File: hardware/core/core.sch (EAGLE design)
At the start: 520 parts, among them IC1 MAX481CSA, IC10 MAX481CSA, IC11 MAX481CSA, IC12 MAX481CSA, IC13 MAX481CSA, IC14 MAX481CSA, IC15 MAX481CSA, IC16 MAX481CSA, IC17 MAX481CSA, IC18 MAX481CSA, IC19 MAX481CSA, IC2 LD117AS12TR, IC20 MAX481CSA, IC21 MAX481CSA, IC22 LD117AS12TR, IC23 LD117AS12TR, IC3 MAX481CSA, IC4 MAX481CSA, IC5 MAX481CSA, IC6 MAX481CSA, IC7 MAX481CSA, IC8 MAX481CSA, IC9 MAX481CSA

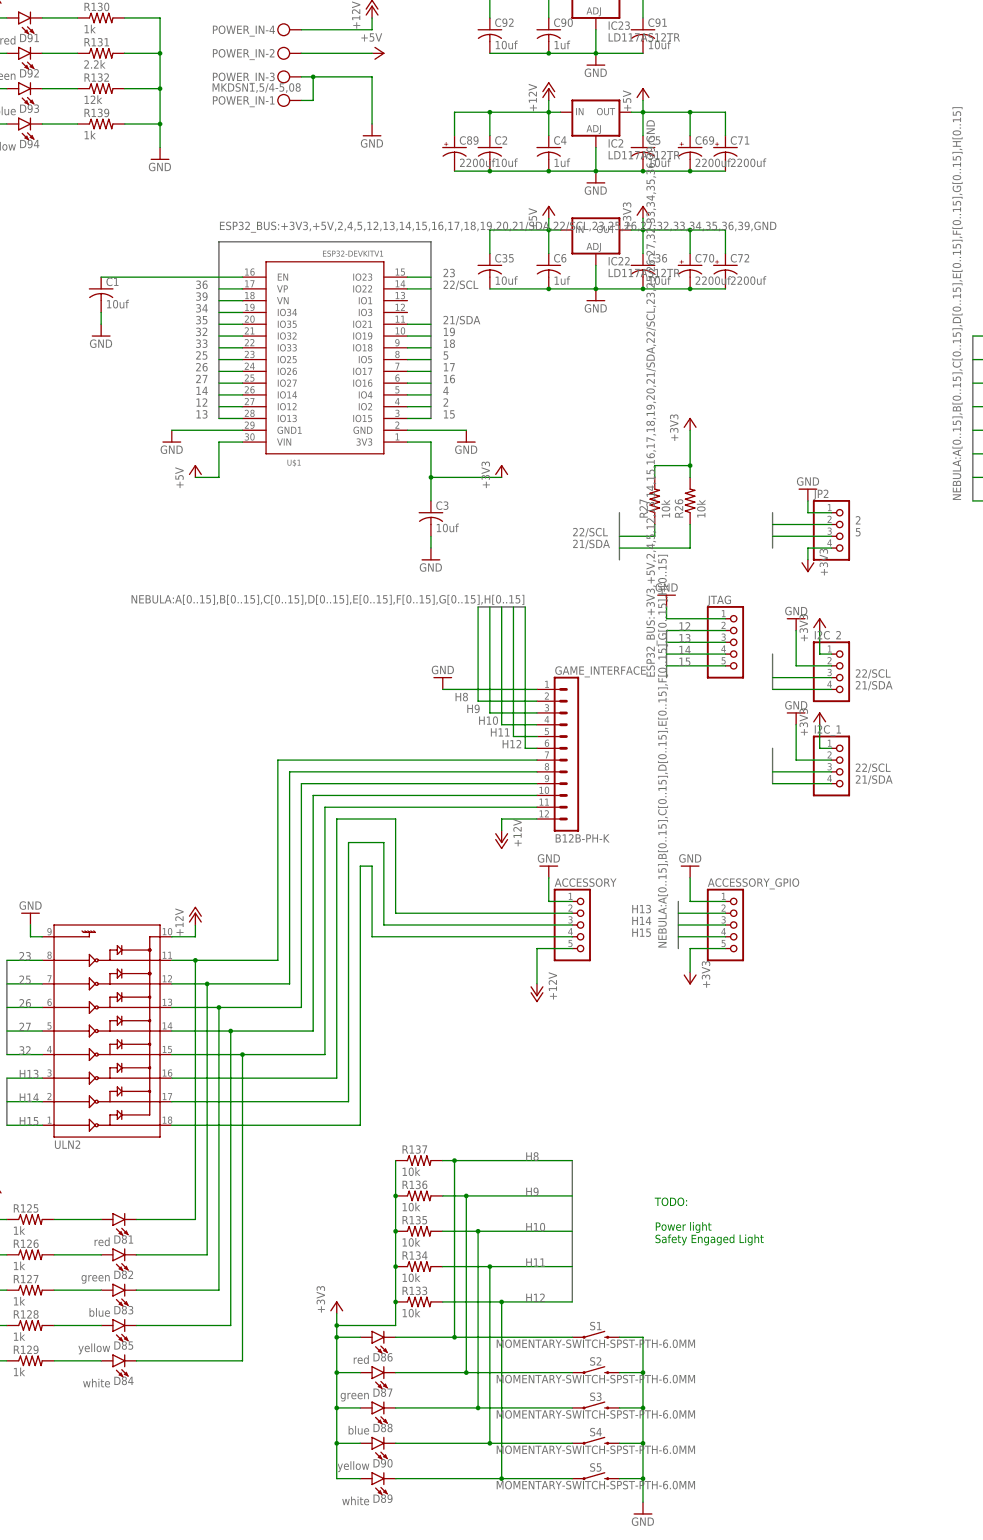
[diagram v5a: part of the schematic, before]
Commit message: Fix for button status resistors & 12v status dim
Fix for button status resistors & 12v status dim
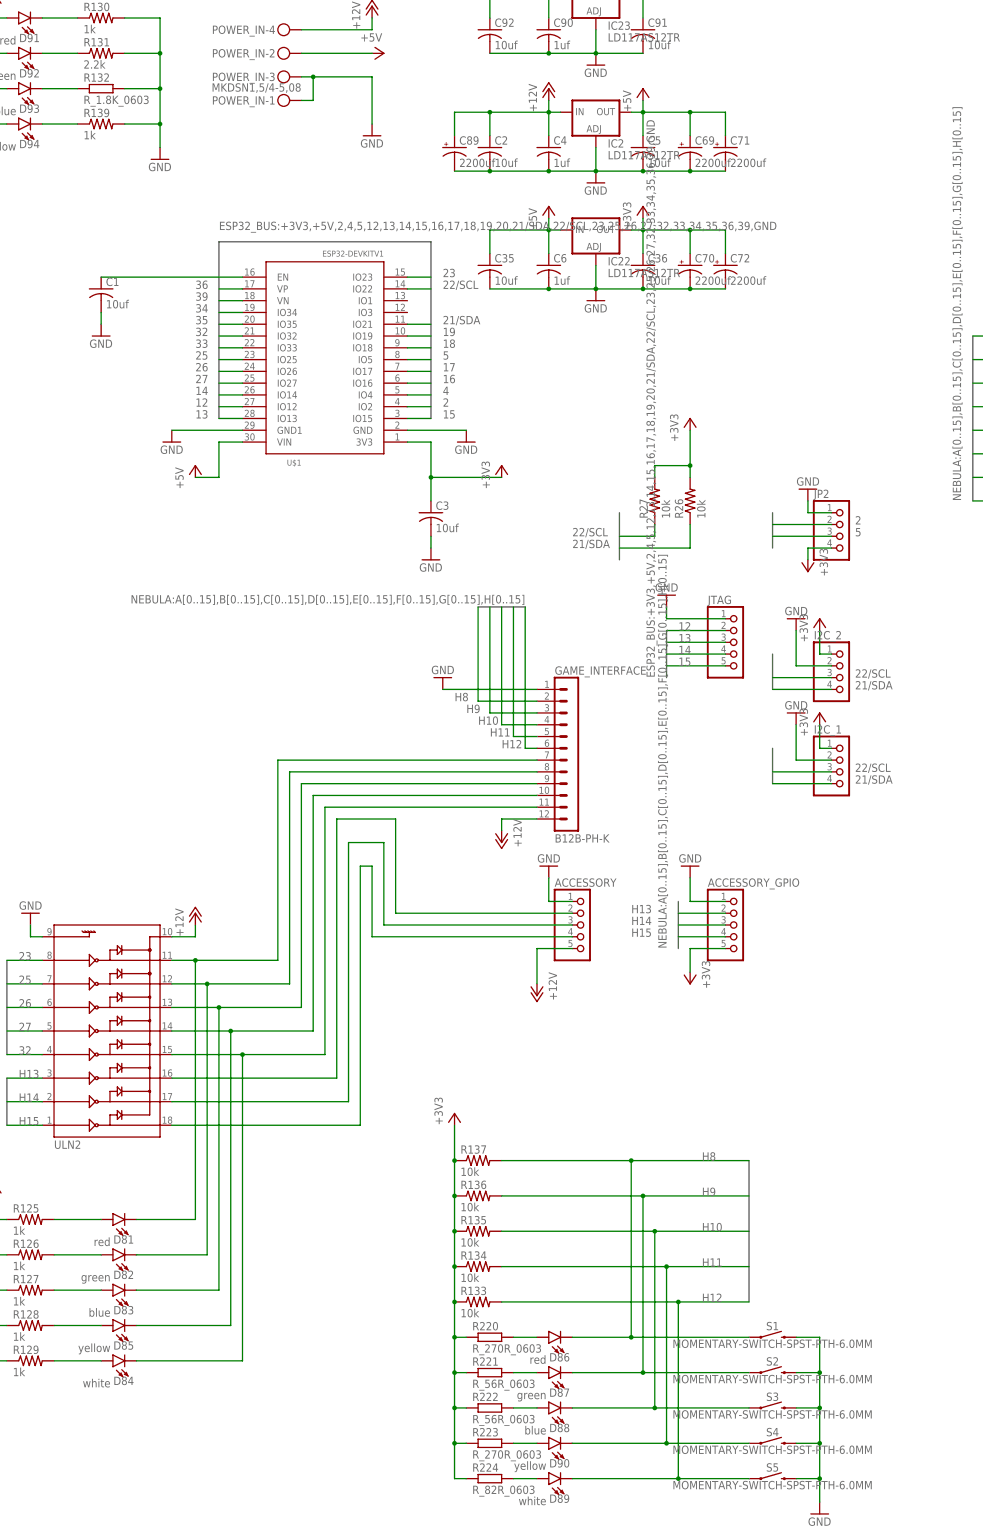
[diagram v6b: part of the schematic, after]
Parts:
- added R220, R223: R_270R_0603, JLC PCB Basic Parts_loc:R_270R_0603
- added R221, R222: R_56R_0603, JLC PCB Basic Parts_loc:R_56R_0603
- added R224: R_82R_0603, JLC PCB Basic Parts_loc:R_82R_0603
- R132: value 12k -> R_1.8K_0603; device rcl:R-US_R0603 -> JLC PCB Basic Parts_loc:R_1.8K_0603; LCSC_PART C22790 -> (none)
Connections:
- new net N$320: D86.A, R220.2
- new net N$321: D87.A, R221.2
- new net N$322: D88.A, R222.2
- new net N$323: D90.A, R223.2
- new net N$324: D89.A, R224.2
- net +3V3: now also R220.1, R221.1, R222.1, R223.1, R224.1; no longer D86.A, D87.A, D88.A, D89.A, D90.A
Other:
- note removed: "TODO: Power light Safety Engaged Light"
- moved on the sheet: D86, D87, D88, D89, D90, R133, R134, R135, R136, R137, S1, S2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

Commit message: progress
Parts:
- added C125: C_1NF/50V_0603, JLC PCB Basic Parts_loc:C_1NF/50V_0603
- added R225: R_1K_0603, JLC PCB Basic Parts_loc:R_1K_0603
- R26, R27: value 10k -> R_2K_0603; device rcl:R-US_R0603 -> JLC PCB Basic Parts_loc:R_2K_0603; LCSC_PART C25804 -> (none)
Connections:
- new net STAR_ENABLE: J1.1, JP1.1, R103.1, R104.1, R105.1, R106.1, R225.2, R54.1, R55.1, R56.1, R57.1, R58.1, R59.1, R60.1, R61.1, R62.1, R63.1, R64.1, R65.1, R67.1, R83.1, R84.1, R85.1, R86.1
- net 13: now also C125.2, R225.1; no longer J1.1, JP1.1, R103.1, R104.1, R105.1, R106.1, R54.1, R55.1, R56.1, R57.1, R58.1, R59.1, R60.1, R61.1, R62.1, R63.1, R64.1, R65.1, R67.1, R83.1, R84.1, R85.1, R86.1
- net GND: now also C125.1
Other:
- moved on the sheet: D81, D82, D83, D84, D85, LEDARRAY, R125, R126, R127, R128, R129, ULN2
